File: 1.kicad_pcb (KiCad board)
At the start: 2 copper layers, 85.1 x 46.4 mm, 44 parts, among them J1 Micro_SD_Card, J10 I2C1, J11 I2C2, J12 B3..9A, J2 USB_B_Micro, J3 Conn_Power, J4 SWD, J5 Protected, J6 SPI1, J7 ADC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

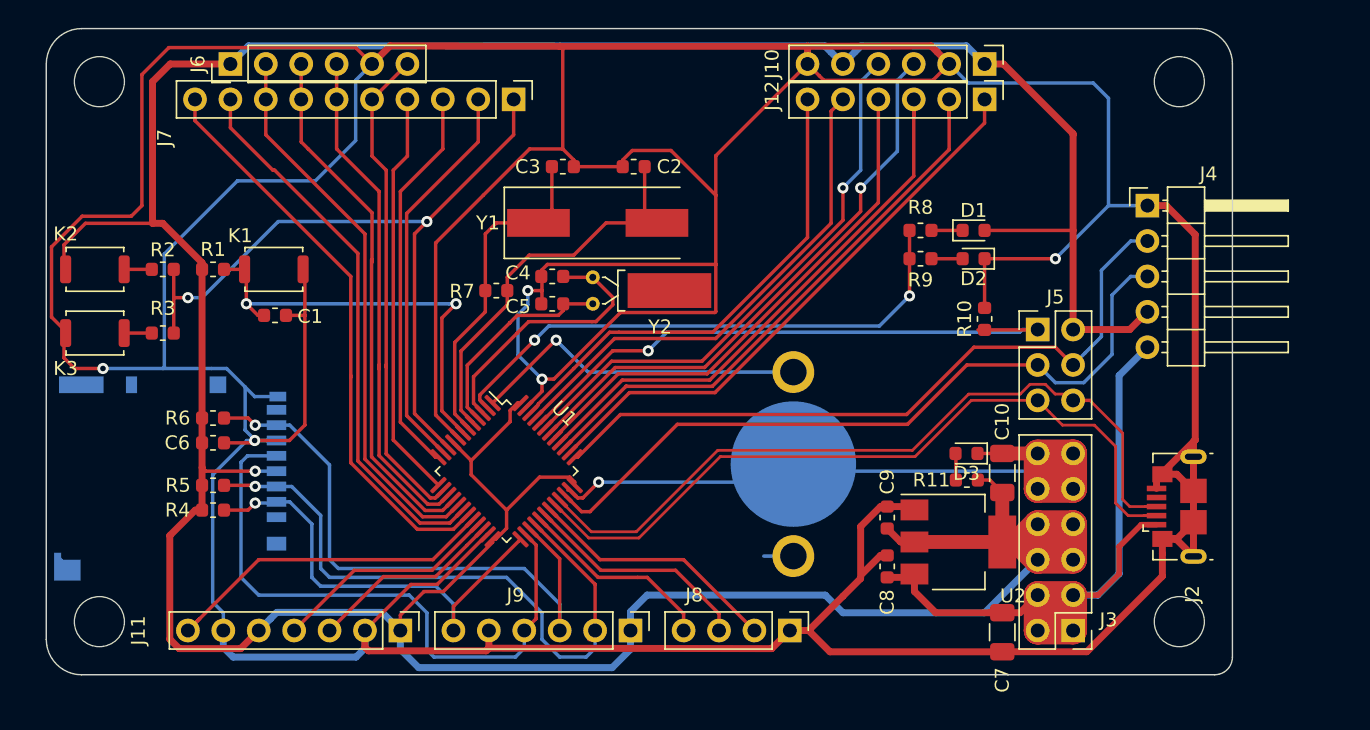
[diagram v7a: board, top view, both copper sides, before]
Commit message: fix DRC warings
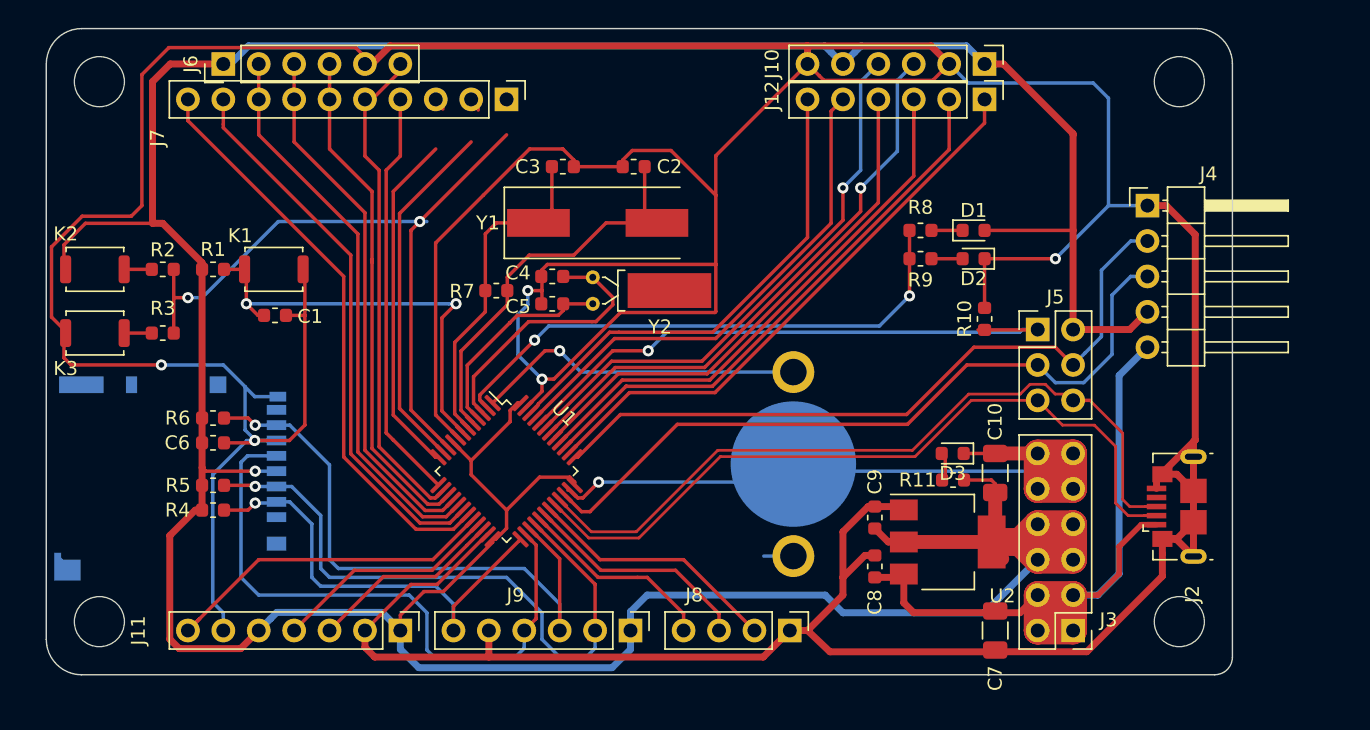
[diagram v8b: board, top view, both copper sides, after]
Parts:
- moved D3 0.99 mm to (161.5, 116.8)
- moved R11 0.99 mm to (161.6, 118.7)
- moved C8 0.89 mm to (156.0, 124.9)
- moved C9 0.89 mm to (156.0, 121.4)
- moved U2 0.76 mm to (161.2, 123.2)
- moved C7 0.52 mm to (164.6, 129.5)
- moved J7 0.51 mm to (129.5, 91.4)
- moved J6 0.51 mm to (109.2, 88.9)
- moved C10 0.51 mm to (164.6, 118.2)
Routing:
- net GND: track 535.6 -> 485.5 mm
- net /PA2: track 29.4 -> 26.0 mm
- net /PA1: track 29.8 -> 27.0 mm
- net /PA0: track 55.0 -> 52.5 mm
- net +5V: track 57.4 -> 58.8 mm
- net +3V3: track 289.7 -> 290.7 mm
- net Net-(BT1-Pad1): track 26.7 -> 25.9 mm
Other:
- board text added: "ADCx CH9..0"
- board text removed: "ADC CH9..0"
